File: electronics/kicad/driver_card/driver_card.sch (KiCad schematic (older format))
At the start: 23 parts, among them J1 CONN_10SMD_MALE, J2 CONN_02, Q1 2N7002, Q2 BSS84, Q3 BSS84, U2 INA194

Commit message: Driver card
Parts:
- removed J2: CONN_02, Connector_PinHeader_2.54mm:PinHeader_1x02_P2.54mm_Vertical, symbol SparkFun-Connectors:CONN_02
- removed Q2: BSS84, Package_TO_SOT_SMD:SOT-23, symbol Transistor_FET:BSS84
- removed R18: 30k, Resistor_SMD:R_0603_1608Metric, symbol SparkFun-Resistors:RESISTOR0402
- removed R19, R2: 1k, Resistor_SMD:R_0603_1608Metric, symbol SparkFun-Resistors:RESISTOR0402
- added C2: 0.1 uF, 0603, symbol SparkFun-Capacitors:4.7UF0603
- added Q2: MMBT4401, digikey-footprints:SOT-23-3, symbol dk_Transistors-Bipolar-BJT-Single:MMBT4401
- added TP1, TP2, TP? (x2): Test_Point, TestPoint:TestPoint_Pad_2.0x2.0mm, symbol Connector:Test_Point
- R10, R12: footprint Resistor_SMD:R_0402_1005Metric -> Resistor_SMD:R_0603_1608Metric
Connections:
- net PULSE_INPUT is gone; now on net ~PULSE_INPUT: Q3.1 (G)
- net pulse_feedback is gone; now on net nsource: J1.5
- net +48V: now also TP1.1
- net 3.3V: now also J1.3, C2.2, Q2.3 (C); no longer J1.2
- net BIAS_PWM: now also J1.10, TP2.1; no longer J1.6
- net CURRENT_SENSE: now also J1.8; no longer J1.4
- net GND: now also C2.1
- net VSOURCE_PWM: now also J1.2; no longer J1.3
- net nsource: now also TP?.1
- net source_supply_feedback: now also C7.2, C8.2, J1.4, Q3.2 (S), Q2.2 (E); no longer J1.8
- net ~PULSE_INPUT: now also J1.6; no longer J1.10
- net VARACTOR_OUT: now reaches C1.2, R10.1, R11.2
- net VARACTOR_OUT: now also TP?.1
- net at C9.1, R14.2: now also Q2.1 (B)
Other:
- note added: "Originally used a P-channel in the linear region,\nbut the BSS84-F in stock SOA is only 0.05 A at DC in linear region\nwow! very surprised!"
- note added: "Two 2.2r because that's all I've got."
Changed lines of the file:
@@
 F 0 "R12" V 5695 1732 45  0000 R CNN
 F 1 "10K" V 5611 1732 45  0000 R CNN
-F 2 "Resistor_SMD:R_0402_1005Metric" H 5600 1950 20  0001 C CNN
+F 2 "Resistor_SMD:R_0603_1608Metric" H 5600 1950 20  0001 C CNN
 F 3 "" H 5600 1800 60  0001 C CNN
 F 4 " " V 5516 1732 60  0000 R CNN "Field4"
@@
 $EndComp
 Wire Wire Line
-	7300 4300 7650 4300
+	7300 4300 7600 4300
 $Comp
 L SparkFun-PowerSymbols:3.3V #SUPPLY0103
@@
 	-1   0    0    1
 $EndComp
-$Comp
-L SparkFun-Resistors:RESISTOR0402 R19
-U 1 1 5F09CB05
-P 7650 4900
-F 0 "R19" V 7745 4832 45  0000 R CNN
-F 1 "1k" V 7661 4832 45  0000 R CNN
-F 2 "Resistor_SMD:R_0603_1608Metric" H 7650 5050 20  0001 C CNN
-F 3 "" H 7650 4900 60  0001 C CNN
-F 4 " " V 7566 4832 60  0000 R CNN "Field4"
-	1    7650 4900
-	0    -1   -1   0
-$EndComp
-$Comp
-L SparkFun-Resistors:RESISTOR0402 R18
-U 1 1 5F09CAFE
-P 7650 4500
-F 0 "R18" V 7745 4432 45  0000 R CNN
-F 1 "30k" V 7661 4432 45  0000 R CNN
-F 2 "Resistor_SMD:R_0603_1608Metric" H 7650 4650 20  0001 C CNN
-F 3 "" H 7650 4500 60  0001 C CNN
-F 4 " " V 7566 4432 60  0000 R CNN "Field4"
-	1    7650 4500
-	0    -1   -1   0
-$EndComp
-$Comp
-L power:GND #PWR0116
-U 1 1 5F09CAF7
-P 7650 5100
-F 0 "#PWR0116" H 7650 5100 30  0001 C CNN
-F 1 "GND" H 7650 5030 30  0001 C CNN
-F 2 "" H 7650 5100 50  0001 C CNN
-F 3 "" H 7650 5100 50  0001 C CNN
-	1    7650 5100
-	1    0    0    -1
-$EndComp
 Wire Wire Line
 	4800 4300 5000 4300
@@
 F 0 "R10" V 6345 1732 45  0000 R CNN
 F 1 "1k" V 6261 1732 45  0000 R CNN
-F 2 "Resistor_SMD:R_0402_1005Metric" H 6250 1950 20  0001 C CNN
+F 2 "Resistor_SMD:R_0603_1608Metric" H 6250 1950 20  0001 C CNN
 F 3 "" H 6250 1800 60  0001 C CNN
 F 4 " " V 6166 1732 60  0000 R CNN "Field4"
@@
 P 6800 2000
 F 0 "R11" V 6895 1932 45  0000 R CNN
-F 1 "30k" V 6811 1932 45  0000 R CNN
+F 1 "30k" H 6811 1932 45  0000 R CNN
 F 2 "Resistor_SMD:R_0603_1608Metric" H 6800 2150 20  0001 C CNN
 F 3 "" H 6800 2000 60  0001 C CNN
@@
 $EndComp
 $Comp
-L Transistor_FET:BSS84 Q2
-U 1 1 5EFB71D5
-P 5200 4400
-F 0 "Q2" V 5543 4400 50  0000 C CNN
-F 1 "BSS84" V 5452 4400 50  0000 C CNN
-F 2 "Package_TO_SOT_SMD:SOT-23" H 5400 4325 50  0001 L CIN
-F 3 "http://assets.nexperia.com/documents/data-sheet/BSS84.pdf" H 5200 4400 50  0001 L CNN
-	1    5200 4400
-	0    1    -1   0
-$EndComp
-$Comp
 L Transistor_FET:BSS84 Q3
 U 1 1 5EFA7A24
@@
 Text GLabel 3350 3150 2    50   Input ~ 0
 VARACTOR_FEEDBACK
-Text GLabel 7650 4700 2    50   Input ~ 0
-pulse_feedback
-Text GLabel 3350 3250 2    50   Input ~ 0
+Text GLabel 3350 2800 2    50   Input ~ 0
 BIAS_PWM
 $Comp
 L SparkFun-PowerSymbols:3.3V #SUPPLY0105
 U 1 1 5F1E0DE3
-P 3350 3650
-F 0 "#SUPPLY0105" H 3400 3650 45  0001 L BNN
-F 1 "3.3V" V 3350 3778 45  0000 L CNN
-F 2 "" V 3308 3777 60  0000 L CNN
-F 3 "" H 3350 3650 60  0001 C CNN
-	1    3350 3650
+P 3350 3550
+F 0 "#SUPPLY0105" H 3400 3550 45  0001 L BNN
+F 1 "3.3V" V 3350 3678 45  0000 L CNN
+F 2 "" V 3308 3677 60  0000 L CNN
+F 3 "" H 3350 3550 60  0001 C CNN
+	1    3350 3550
 	0    1    1    0
 $EndComp
@@
 	0    -1   -1   0
 $EndComp
-Text GLabel 6700 5000 3    50   Input ~ 0
-PULSE_INPUT
-Text GLabel 3350 2800 2    50   Input ~ 0
-~PULSE_INPUT
 Text GLabel 5600 2000 0    50   Input ~ 0
 ~VARACTOR_PWM
@@
 Text GLabel 7100 3150 1    50   Input ~ 0
 CURRENT_SENSE
-Text GLabel 3350 3450 2    50   Input ~ 0
+Text GLabel 3350 3050 2    50   Input ~ 0
 CURRENT_SENSE
 Text GLabel 5200 5650 3    50   Input ~ 0
 VSOURCE_PWM
-Text GLabel 3350 3550 2    50   Input ~ 0
+Text GLabel 3350 3650 2    50   Input ~ 0
 VSOURCE_PWM
 $Comp
@@
 	1    0    0    -1
 $EndComp
-Text GLabel 3350 3050 2    50   Input ~ 0
+Text GLabel 3350 3450 2    50   Input ~ 0
 source_supply_feedback
 Text GLabel 3350 3350 2    50   Input ~ 0
@@
 Wire Wire Line
 	3350 2850 3350 2800
-$Comp
-L SparkFun-Connectors:CONN_02 J2
-U 1 1 5F20BF2F
-P 3350 1950
-F 0 "J2" H 3308 2360 45  0000 C CNN
-F 1 "CONN_02" H 3308 2276 45  0000 C CNN
-F 2 "Connector_PinHeader_2.54mm:PinHeader_1x02_P2.54mm_Vertical" H 3350 2200 20  0001 C CNN
-F 3 "" H 3350 1950 50  0001 C CNN
-F 4 "XXX-00000" H 3308 2181 60  0000 C CNN "Field4"
-	1    3350 1950
-	1    0    0    -1
-$EndComp
 $Comp
 L power2:+48V #PWR0103
@@
 	1    0    0    -1
 $EndComp
-$Comp
-L power:GND #PWR0106
-U 1 1 5F212AC1
-P 3450 1950
-F 0 "#PWR0106" H 3450 1950 30  0001 C CNN
-F 1 "GND" H 3450 1880 30  0001 C CNN
-F 2 "" H 3450 1950 50  0001 C CNN
-F 3 "" H 3450 1950 50  0001 C CNN
-	1    3450 1950
-	0    -1   -1   0
-$EndComp
 Wire Wire Line
 	5400 4300 5650 4300
-$Comp
-L SparkFun-Resistors:RESISTOR0402 R2
-U 1 1 5F2086A8
-P 5650 5000
-F 0 "R2" V 5745 4932 45  0000 R CNN
-F 1 "1k" V 5661 4932 45  0000 R CNN
-F 2 "Resistor_SMD:R_0603_1608Metric" H 5650 5150 20  0001 C CNN
-F 3 "" H 5650 5000 60  0001 C CNN
-F 4 " " V 5566 4932 60  0000 R CNN "Field4"
-	1    5650 5000
-	0    -1   -1   0
-$EndComp
-Text GLabel 5650 5200 2    50   Input ~ 0
+Text GLabel 5650 4800 2    50   Input ~ 0
 source_supply_feedback
 $Comp
@@
 Wire Wire Line
 	5650 4300 5850 4300
+Text Notes 7850 4000 0    50   ~ 0
+Two 2.2r because that's all I've got.
+Text Notes 8000 6150 0    50   ~ 0
+Originally used a P-channel in the linear region,\nbut the BSS84-F in stock SOA is only 0.05 A at DC in linear region\nwow! very surprised!
+$Comp
+L dk_Transistors-Bipolar-BJT-Single:MMBT4401 Q2
+U 1 1 5EE95D01
+P 5200 4400
+F 0 "Q2" V 5547 4400 60  0000 C CNN
+F 1 "MMBT4401" V 5441 4400 60  0000 C CNN
+F 2 "digikey-footprints:SOT-23-3" H 5400 4600 60  0001 L CNN
+F 3 "https://www.fairchildsemi.com/datasheets/2N/2N4401.pdf" H 5400 4700 60  0001 L CNN
+F 4 "MMBT4401FSCT-ND" H 5400 4800 60  0001 L CNN "Digi-Key_PN"
+F 5 "MMBT4401" H 5400 4900 60  0001 L CNN "MPN"
+F 6 "Discrete Semiconductor Products" H 5400 5000 60  0001 L CNN "Category"
+F 7 "Transistors - Bipolar (BJT) - Single" H 5400 5100 60  0001 L CNN "Family"
+F 8 "https://www.fairchildsemi.com/datasheets/2N/2N4401.pdf" H 5400 5200 60  0001 L CNN "DK_Datasheet_Link"
+F 9 "/product-detail/en/on-semiconductor/MMBT4401/MMBT4401FSCT-ND/458974" H 5400 5300 60  0001 L CNN "DK_Detail_Page"
+F 10 "TRANS NPN 40V 0.6A SOT-23" H 5400 5400 60  0001 L CNN "Description"
+F 11 "ON Semiconductor" H 5400 5500 60  0001 L CNN "Manufacturer"
+F 12 "Active" H 5400 5600 60  0001 L CNN "Status"
+	1    5200 4400
+	0    -1   -1   0
+$EndComp
+Text GLabel 7600 4500 2    50   Input ~ 0
+pulse_feedback
+Wire Wire Line
+	7600 4300 7600 4500
+Connection ~ 7600 4300
+Wire Wire Line
+	7600 4300 7650 4300
+$Comp
+L SparkFun-Capacitors:4.7UF0603 C2
+U 1 1 5EEA123E
+P 4800 4400
+F 0 "C2" V 4566 4450 45  0000 C CNN
+F 1 "0.1 uF" V 4650 4450 45  0000 C CNN
+F 2 "0603" H 4800 4650 20  0001 C CNN
+F 3 "" H 4800 4400 50  0001 C CNN
+F 4 "" H 4908 4366 60  0000 L CNN "Field4"
+	1    4800 4400
+	-1   0    0    1
+$EndComp
+Connection ~ 4800 4300
+$Comp
+L power:GND #PWR0102
+U 1 1 5EEA228C
+P 4800 4600
+F 0 "#PWR0102" H 4800 4600 30  0001 C CNN
+F 1 "GND" H 4800 4530 30  0001 C CNN
+F 2 "" H 4800 4600 50  0001 C CNN
+F 3 "" H 4800 4600 50  0001 C CNN
+	1    4800 4600
+	1    0    0    -1
+$EndComp
+Text GLabel 6700 5000 3    50   Input ~ 0
+~PULSE_INPUT
+Text GLabel 4650 3250 0    50   Input ~ 0
+BIAS_PWM
+$Comp
+L Connector:Test_Point TP1
+U 1 1 5EEB43DF
+P 3450 1850
+F 0 "TP1" H 3508 1968 50  0000 L CNN
+F 1 "Test_Point" H 3508 1877 50  0000 L CNN
+F 2 "TestPoint:TestPoint_Pad_2.0x2.0mm" H 3650 1850 50  0001 C CNN
+F 3 "~" H 3650 1850 50  0001 C CNN
+	1    3450 1850
+	0    -1   -1   0
+$EndComp
+$Comp
+L Connector:Test_Point TP2
+U 1 1 5EEBBE60
+P 4650 3250
+F 0 "TP2" H 4708 3368 50  0000 L CNN
+F 1 "Test_Point" H 4708 3277 50  0000 L CNN
+F 2 "TestPoint:TestPoint_Pad_2.0x2.0mm" H 4850 3250 50  0001 C CNN
+F 3 "~" H 4850 3250 50  0001 C CNN
+	1    4650 3250
+	0    1    1    0
+$EndComp
+Text GLabel 3350 3250 2    50   Input ~ 0
+~PULSE_INPUT
+$Comp
+L Connector:Test_Point TP?
+U 1 1 5EEC794F
+P 7400 1550
+F 0 "TP?" H 7458 1668 50  0000 L CNN
+F 1 "Test_Point" H 7458 1577 50  0000 L CNN
+F 2 "TestPoint:TestPoint_Pad_2.0x2.0mm" H 7600 1550 50  0001 C CNN
+F 3 "~" H 7600 1550 50  0001 C CNN
+	1    7400 1550
+	0    1    1    0
+$EndComp
+Connection ~ 6800 1800
+Text GLabel 6800 1800 2    50   Input ~ 0
+VARACTOR_OUT
+Text GLabel 7400 1550 0    50   Input ~ 0
+VARACTOR_OUT
+$Comp
+L Connector:Test_Point TP?
+U 1 1 5EECA2A9
+P 8750 4350
+F 0 "TP?" H 8808 4468 50  0000 L CNN
+F 1 "Test_Point" H 8808 4377 50  0000 L CNN
+F 2 "TestPoint:TestPoint_Pad_2.0x2.0mm" H 8950 4350 50  0001 C CNN
+F 3 "~" H 8950 4350 50  0001 C CNN
+	1    8750 4350
+	0    1    1    0
+$EndComp
+Text GLabel 8750 4350 0    50   Input ~ 0
+nsource
 $EndSCHEMATC

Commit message: Teensy
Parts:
- gave numbers to parts that had none: 2
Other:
- note added: "Originally used a P-channel in the linear region,\nbut at 3.3v, the Safe Operating Area at DC of the BSS84-F \nonly goes up to 50 mA - remarkable!"
- note added: "We could use an op-amp to provide the feedback \nfor both of these circuits, lessening the load on the Teensy,\nbut whatever"
- note removed: "Originally used a P-channel in the linear region,\nbut the BSS84-F in stock SOA is only 0.05 A at DC in linear region\nwow! very surprised!"
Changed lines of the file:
@@
 Text Notes 7850 4000 0    50   ~ 0
 Two 2.2r because that's all I've got.
-Text Notes 8000 6150 0    50   ~ 0
-Originally used a P-channel in the linear region,\nbut the BSS84-F in stock SOA is only 0.05 A at DC in linear region\nwow! very surprised!
+Text Notes 7600 5850 0    50   ~ 0
+Originally used a P-channel in the linear region,\nbut at 3.3v, the Safe Operating Area at DC of the BSS84-F \nonly goes up to 50 mA - remarkable!
 $Comp
 L dk_Transistors-Bipolar-BJT-Single:MMBT4401 Q2
@@
 ~PULSE_INPUT
 $Comp
-L Connector:Test_Point TP?
+L Connector:Test_Point TP3
 U 1 1 5EEC794F
 P 7400 1550
-F 0 "TP?" H 7458 1668 50  0000 L CNN
+F 0 "TP3" H 7458 1668 50  0000 L CNN
 F 1 "Test_Point" H 7458 1577 50  0000 L CNN
 F 2 "TestPoint:TestPoint_Pad_2.0x2.0mm" H 7600 1550 50  0001 C CNN
@@
 	0    1    1    0
 $EndComp
-Connection ~ 6800 1800
 Text GLabel 6800 1800 2    50   Input ~ 0
 VARACTOR_OUT
@@
 VARACTOR_OUT
 $Comp
-L Connector:Test_Point TP?
+L Connector:Test_Point TP4
 U 1 1 5EECA2A9
 P 8750 4350
-F 0 "TP?" H 8808 4468 50  0000 L CNN
+F 0 "TP4" H 8808 4468 50  0000 L CNN
 F 1 "Test_Point" H 8808 4377 50  0000 L CNN
 F 2 "TestPoint:TestPoint_Pad_2.0x2.0mm" H 8950 4350 50  0001 C CNN
@@
 Text GLabel 8750 4350 0    50   Input ~ 0
 nsource
+Text Notes 7900 1150 0    50   ~ 0
+We could use an op-amp to provide the feedback \nfor both of these circuits, lessening the load on the Teensy,\nbut whatever
 $EndSCHEMATC

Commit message: Power integration,
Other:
- note added: "5 ohms * 0.1 uF = 500 ns - that filter cap on the oscillator has to go\n- some nF should be okay"
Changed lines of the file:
@@
 Text Notes 7900 1150 0    50   ~ 0
 We could use an op-amp to provide the feedback \nfor both of these circuits, lessening the load on the Teensy,\nbut whatever
+Text Notes 7900 3550 0    50   ~ 0
+5 ohms * 0.1 uF = 500 ns - that filter cap on the oscillator has to go\n- some nF should be okay
 $EndSCHEMATC

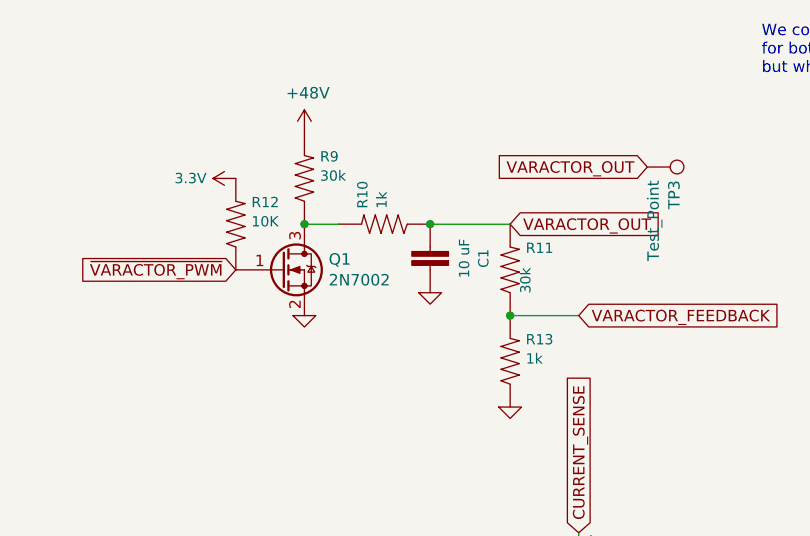
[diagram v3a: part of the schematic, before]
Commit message: Replaced decoupling caps
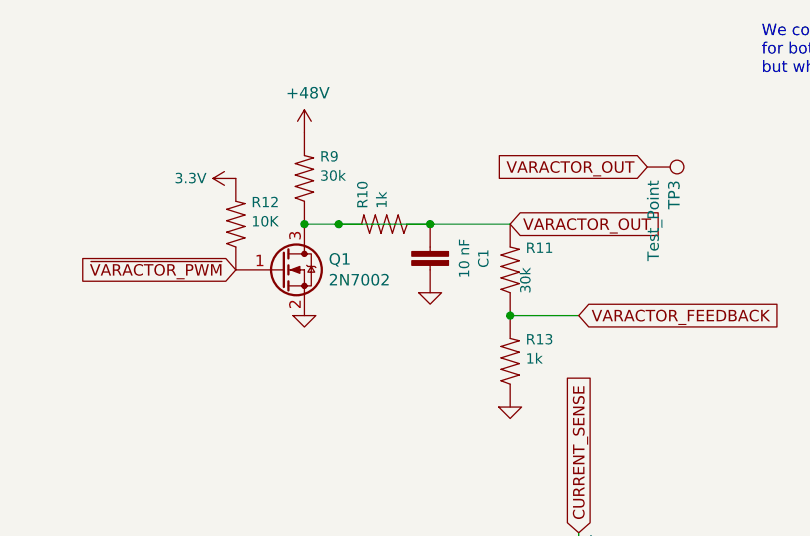
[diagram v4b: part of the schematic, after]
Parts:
- C1: value 10 uF -> 10 nF
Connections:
- net VARACTOR_OUT: now also Q1.3 (D), R10.2, R9.1
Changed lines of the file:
@@
 P 6450 1900
 F 0 "C1" V 6216 1950 45  0000 C CNN
-F 1 "10 uF" V 6300 1950 45  0000 C CNN
+F 1 "10 nF" V 6300 1950 45  0000 C CNN
 F 2 "0603" H 6450 2150 20  0001 C CNN
 F 3 "" H 6450 1900 50  0001 C CNN
@@
 Text Notes 7900 3550 0    50   ~ 0
 5 ohms * 0.1 uF = 500 ns - that filter cap on the oscillator has to go\n- some nF should be okay
+Wire Wire Line
+	6050 1800 6450 1800
+Connection ~ 6050 1800
 $EndSCHEMATC

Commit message: Reorganized
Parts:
- added C?: 0.1 uF, 0603, symbol SparkFun-Capacitors:4.7UF0603
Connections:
- net +48V: now also C?.2
- net GND: now also C?.1
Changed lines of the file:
@@
 	6050 1800 6450 1800
 Connection ~ 6050 1800
+$Comp
+L SparkFun-Capacitors:4.7UF0603 C?
+U 1 1 5EEF63C1
+P 6400 1400
+F 0 "C?" V 6166 1450 45  0000 C CNN
+F 1 "0.1 uF" V 6250 1450 45  0000 C CNN
+F 2 "0603" H 6400 1650 20  0001 C CNN
+F 3 "" H 6400 1400 50  0001 C CNN
+F 4 "" H 6508 1366 60  0000 L CNN "Field4"
+	1    6400 1400
+	0    1    1    0
+$EndComp
+$Comp
+L power2:+48V #PWR?
+U 1 1 5EEF78EF
+P 6300 1400
+F 0 "#PWR?" H 6300 1250 50  0001 C CNN
+F 1 "+48V" H 6315 1573 50  0000 C CNN
+F 2 "" H 6300 1400 50  0001 C CNN
+F 3 "" H 6300 1400 50  0001 C CNN
+	1    6300 1400
+	1    0    0    -1
+$EndComp
+$Comp
+L power:GND #PWR?
+U 1 1 5EEF7C9B
+P 6600 1400
+F 0 "#PWR?" H 6600 1400 30  0001 C CNN
+F 1 "GND" H 6600 1330 30  0001 C CNN
+F 2 "" H 6600 1400 50  0001 C CNN
+F 3 "" H 6600 1400 50  0001 C CNN
+	1    6600 1400
+	1    0    0    -1
+$EndComp
 $EndSCHEMATC
